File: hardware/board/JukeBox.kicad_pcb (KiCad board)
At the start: 2 copper layers, 90 x 90 mm, 72 parts, among them J1 USB4105-GF-A, J2 Conn_01x03, J3 Conn_01x04, J4 Conn_01x08, J5 Conn_01x01, J6 Conn_01x03, J7 Conn_01x03, J8 Conn_01x01, SW1 SW_SPST, SW10 SW_SPST, SW11 SW_SPST, SW12 SW_SPST, SW2 SW_SPST, SW3 SW_SPST, SW4 SW_SPST, SW5 SW_SPST, SW6 SW_SPST, SW7 SW_SPST, SW8 SW_SPST, SW9 SW_SPST, U1 NCP1117-3.3_SOT223, U2 W25Q128JVS, U3 RP2040, Y1 ABLS-12.000MHZ-B4-T

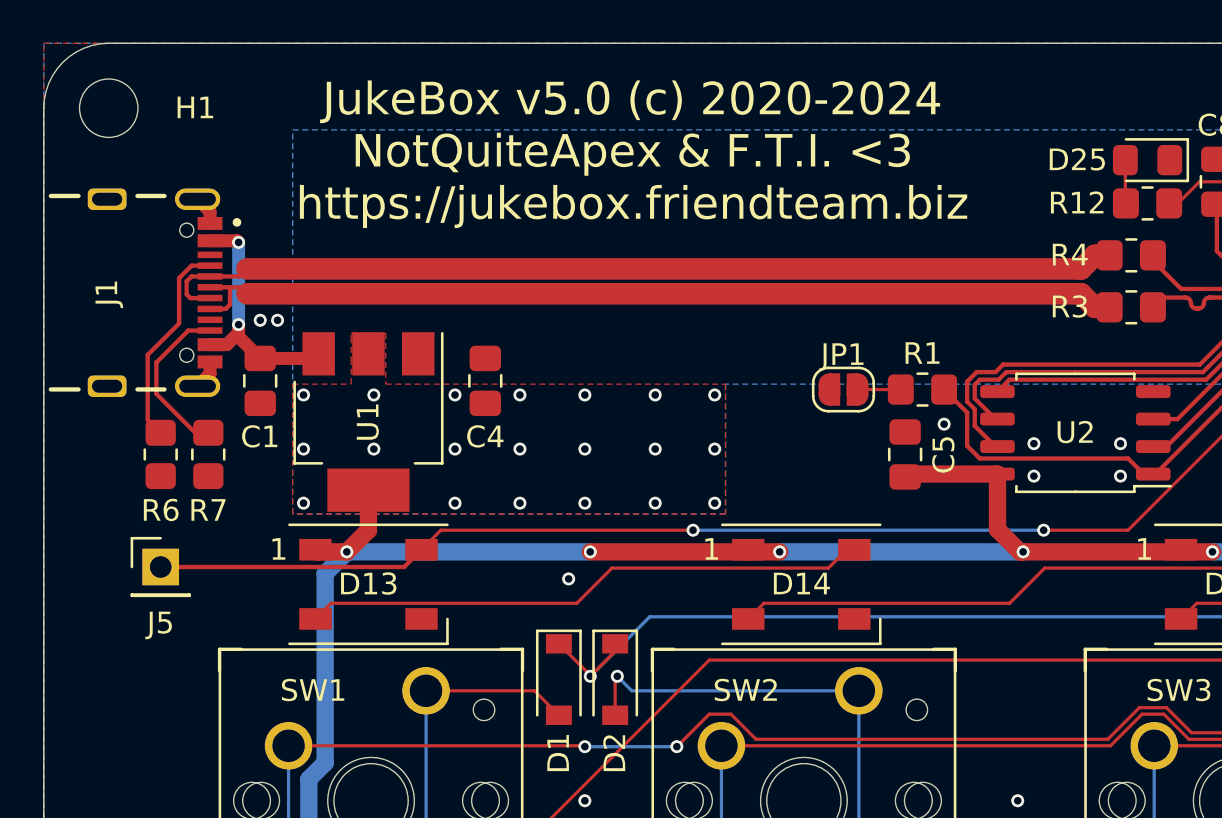
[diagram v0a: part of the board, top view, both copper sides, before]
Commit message: move usb on board downward for leg spacing
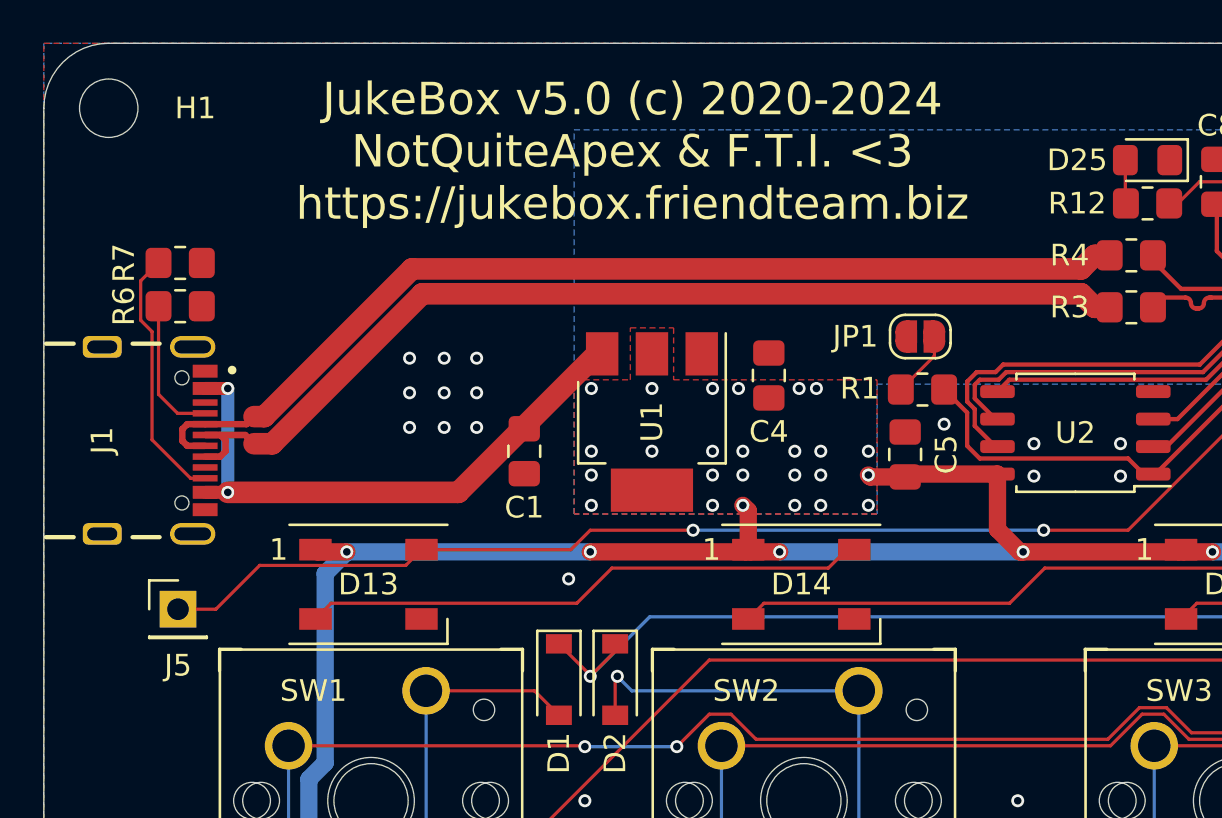
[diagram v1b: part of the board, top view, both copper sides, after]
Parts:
- moved C4 13.1 mm to (119.0, 122.2)
- moved U1 13.1 mm to (113.6, 124.3)
- moved C1 12.6 mm to (107.7, 125.7)
- moved R7 8.94 mm to (91.8, 117.0), turned to 0 degrees
- moved R6 6.91 mm to (91.8, 119.0), turned to 0 degrees
- moved J1 6.83 mm to (88.2, 125.2)
- moved JP1 4.31 mm to (126.0, 120.4)
- moved J5 2.11 mm to (91.7, 133.0)
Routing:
- net VBUS: track 11.5 -> 26.8 mm
- net Net-(J1-PadB5): track 7.69 -> 11.9 mm
- net /USB_D+: track 43.8 -> 47.7 mm
- net Net-(J1-PadA5): track 9.66 -> 6.59 mm
- net /USB_D-: track 44.9 -> 47.9 mm
- net GND: track 11.1 -> 8.39 mm, vias 34 -> 41
- net /~{USB_BOOT}: track 2.00 -> 3.09 mm
- net +3V3: track 248.3 -> 248.9 mm, vias 41 -> 46

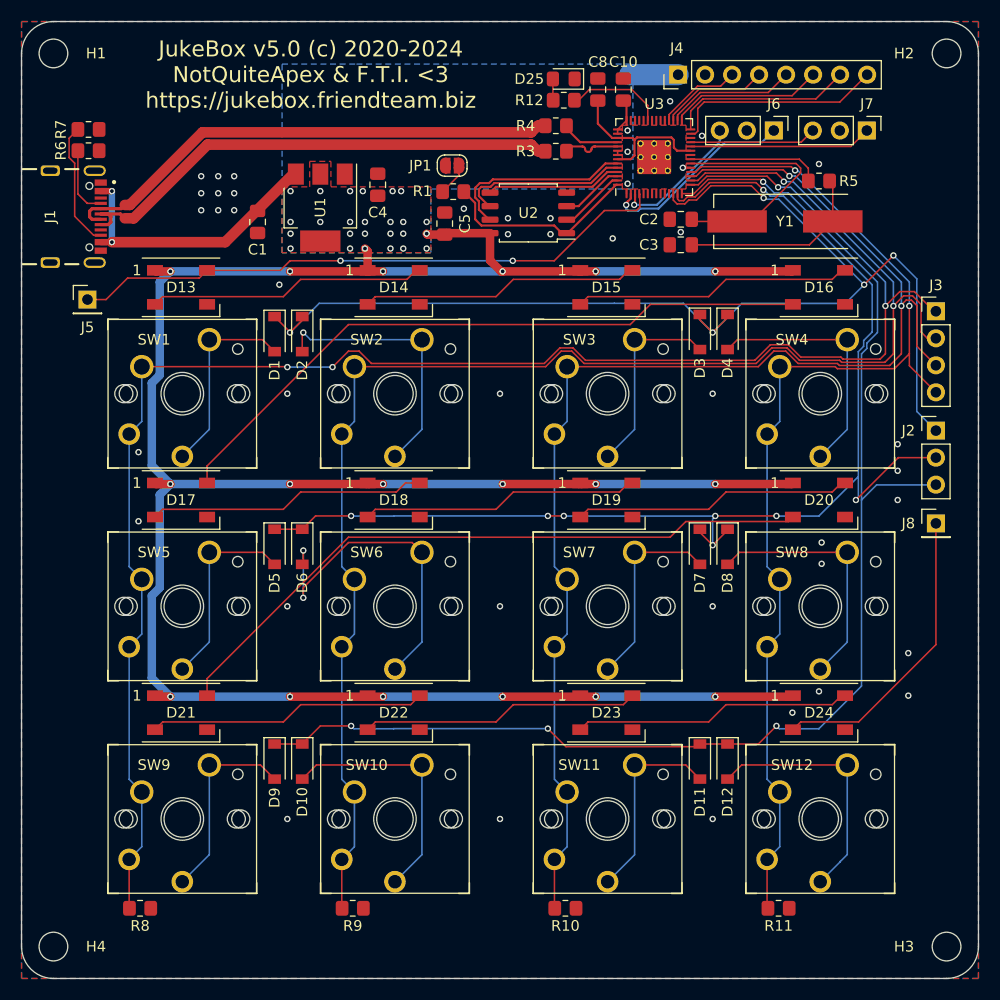
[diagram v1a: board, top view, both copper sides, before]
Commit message: update routing for usb, add logos
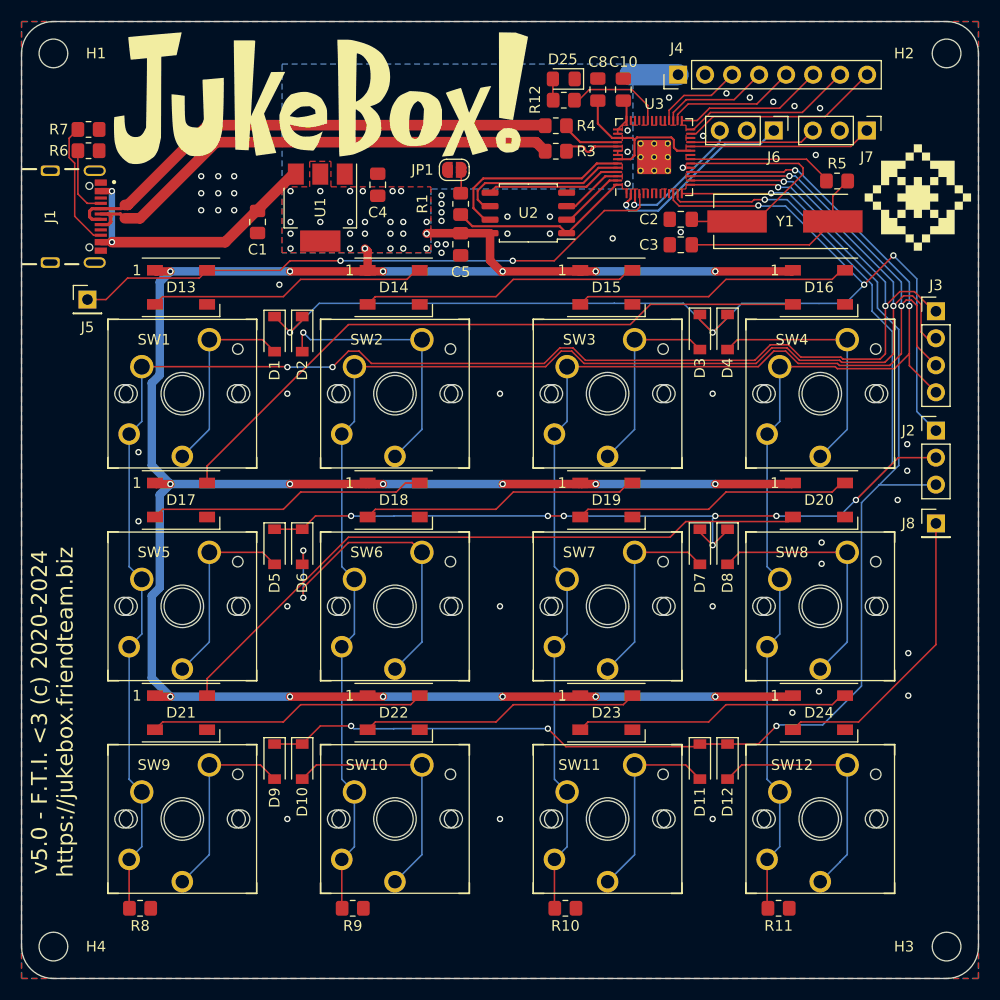
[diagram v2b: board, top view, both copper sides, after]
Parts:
- added G***: LOGO, RP2040_minimal:FTI, F.Cu at (169.8, 123.4)
- added G1: LOGO, RP2040_minimal:JukeBox, F.Cu at (113.6, 114.0)
- moved C5 2.46 mm to (126.8, 127.8), turned to -90 degrees
- moved R5 1.70 mm to (162.2, 121.8)
- moved R1 1.35 mm to (126.8, 124.0), turned to -90 degrees
- moved JP1 0.45 mm to (126.2, 120.8)
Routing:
- net /GPIO11: track 128.5 -> 126.6 mm
- net /QSPI_SS: track 18.9 -> 17.4 mm
- net /GPIO9: track 112.0 -> 110.6 mm
- net /GPIO16: track 20.1 -> 18.9 mm
- net /XOUT: track 12.6 -> 13.7 mm
- net /GPIO17: track 17.2 -> 16.2 mm
- net /~{USB_BOOT}: track 3.09 -> 2.22 mm
- net /GPIO10: track 117.5 -> 116.7 mm
- net /GPIO12: track 162.5 -> 161.9 mm
- net /GPIO13: track 144.7 -> 144.0 mm
- net /XIN: track 23.2 -> 23.7 mm
- net /USB_D+: track 47.7 -> 47.2 mm
- net GND: vias 41 -> 52
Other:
- board text added: "v5.0 - F.T.I. <3 (c) 2020-2024 https://jukebox.friendteam.biz"
- board text removed: "JukeBox v5.0 (c) 2020-2024 NotQuiteApex & F.T.I. <3 https://jukebox.friendteam.biz"
